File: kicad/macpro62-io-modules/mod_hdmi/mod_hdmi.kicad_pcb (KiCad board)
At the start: 2 copper layers, 43.4 x 9.4 mm, 5 parts, among them J1 MOD-H - HOAUC HYC79-HDMIA19-1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, J2 DF40C-50DP-0.4V(51) C424645 -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, U1 24C02 WLCSP-4 ID EEPROM @0x50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

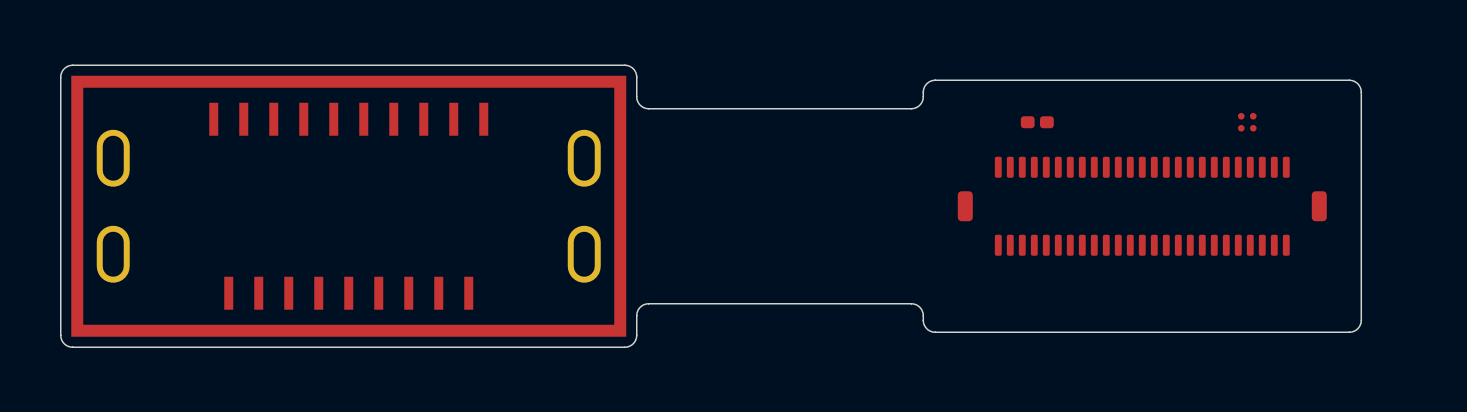
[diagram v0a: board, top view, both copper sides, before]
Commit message: I/O plate: centre + corner M1.6 frame screws, screwpt variant, plate fixes, module routing, ESD
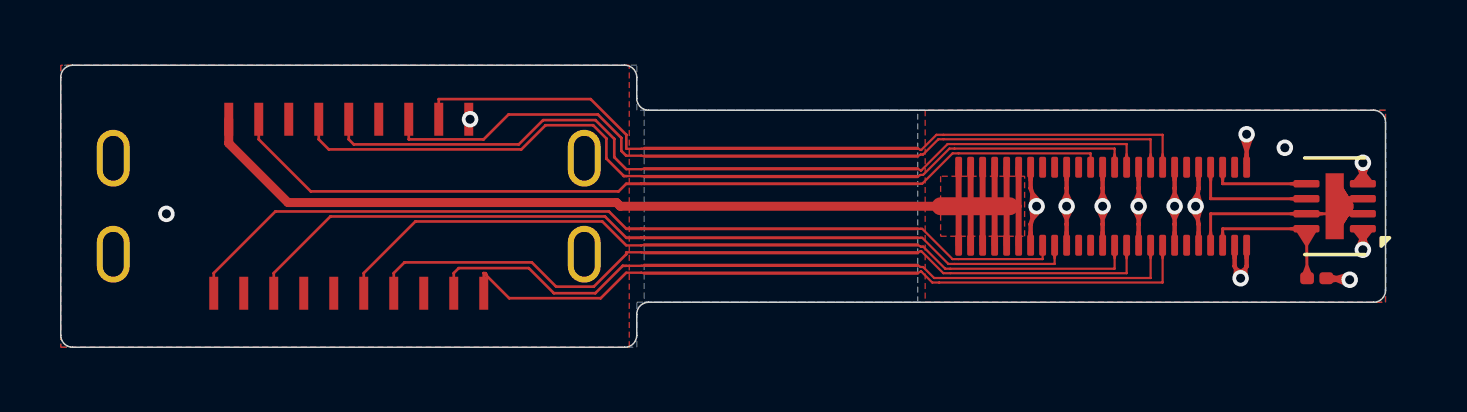
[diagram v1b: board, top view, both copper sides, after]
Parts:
- removed G1: sleeve GND ring (SUS304 0.2 sleeve, bonded to the shell), MP62_MOD:MP62_MOD_Sleeve_GND_Ring_HDMI
- C1: value 100nF 0201 (3V3_MOD) -> 100nF 0201 X5R 10V (3V3_MOD)
- J2: value DF40C-50DP-0.4V(51) C424645 -> main-board JMn DF40C-50DS (PMI-50 pinout) -> DF40C-50DP-0.4V(51) C424645 -> JMn DF40C-50DS (PMI-50 v2)
- U1: value 24C02 WLCSP-4 ID EEPROM @0x50 (MOD ID / type / rev / serial) -> BL24C02F-NTRC (C2828222) 24C02 ID EEPROM @0x50; footprint MP62_MOD:MP62_WLCSP-4_0.8x0.8_P0.4_EEPROM -> MP62_MOD:DFN-8-1EP_2x3mm_P0.5mm_EP0.61x2.2mm
- moved C1 10.7 mm to (132.3, 102.4)
- moved U1 4.04 mm to (132.9, 100.0), turned to 180 degrees
- moved J2 1.32 mm to (125.1, 100.0)
- turned J1 to 180 degrees
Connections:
- C1 pad 1: (no net) -> 3V3_MOD
- C1 pad 2: (no net) -> GND
- J1 pad 1: (no net) -> D2_P
- J1 pad 10: (no net) -> CK_P
- J1 pad 11: (no net) -> GND
- J1 pad 12: (no net) -> CK_N
- J1 pad 15: (no net) -> DDC_SCL
- J1 pad 16: (no net) -> DDC_SDA
- J1 pad 17: (no net) -> GND
- J1 pad 18: (no net) -> VBUS
- J1 pad 19: (no net) -> HPD
- J1 pad 2: (no net) -> GND
- J1 pad 3: (no net) -> D2_N
- J1 pad 4: (no net) -> D1_P
- J1 pad 5: (no net) -> GND
- J1 pad 6: (no net) -> D1_N
- J1 pad 7: (no net) -> D0_P
- J1 pad 8: (no net) -> GND
- J1 pad 9: (no net) -> D0_N
- J1 pad S: (no net) -> GND
- J2 pad 1: (no net) -> VBUS
- J2 pad 10: (no net) -> VBUS
- J2 pad 11: (no net) -> VBUS
- J2 pad 12: (no net) -> VBUS
- J2 pad 13: (no net) -> GND
- J2 pad 14: (no net) -> GND
- J2 pad 16: (no net) -> HPD
- J2 pad 18: (no net) -> DDC_SCL
- J2 pad 19: (no net) -> GND
- J2 pad 2: (no net) -> VBUS
- J2 pad 20: (no net) -> GND
- J2 pad 23: (no net) -> DDC_SDA
- J2 pad 25: (no net) -> GND
- J2 pad 26: (no net) -> GND
- J2 pad 27: (no net) -> CK_N
- J2 pad 28: (no net) -> D0_N
- J2 pad 29: (no net) -> CK_P
- J2 pad 3: (no net) -> VBUS
- J2 pad 30: (no net) -> D0_P
- J2 pad 31: (no net) -> GND
- J2 pad 32: (no net) -> GND
- J2 pad 33: (no net) -> D1_N
- J2 pad 34: (no net) -> D2_N
- J2 pad 35: (no net) -> D1_P
- J2 pad 36: (no net) -> D2_P
- J2 pad 37: (no net) -> GND
- J2 pad 38: (no net) -> GND
- J2 pad 4: (no net) -> VBUS
- J2 pad 41: (no net) -> GND
- J2 pad 42: (no net) -> GND
- J2 pad 43: (no net) -> ID_SCL
- J2 pad 44: (no net) -> GND
- J2 pad 45: (no net) -> ID_SDA
- J2 pad 46: (no net) -> 3V3_MOD
- J2 pad 48: (no net) -> GND
- J2 pad 49: (no net) -> GND
- J2 pad 5: (no net) -> VBUS
- J2 pad 50: (no net) -> GND
- J2 pad 6: (no net) -> VBUS
- J2 pad 7: (no net) -> VBUS
- J2 pad 8: (no net) -> VBUS
- J2 pad 9: (no net) -> VBUS
- U1 pad 1: (no net) -> GND
- U1 pad 2: (no net) -> GND
- U1 pad 3: (no net) -> GND
- U1 pad 4: (no net) -> GND
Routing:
- net VBUS: track 0.00 -> 43.6 mm
- net HPD: track 0.00 -> 30.3 mm
- net DDC_SDA: track 0.00 -> 30.1 mm
- net CK_N: track 0.00 -> 29.8 mm
- net CK_P: track 0.00 -> 29.2 mm
- net DDC_SCL: track 0.00 -> 28.8 mm
- net GND: track 0.00 -> 28.3 mm, vias 0 -> 14
- net D0_N: track 0.00 -> 27.8 mm
- net D1_N: track 0.00 -> 27.7 mm
- net D0_P: track 0.00 -> 27.3 mm
- net D1_P: track 0.00 -> 27.1 mm
- net D2_N: track 0.00 -> 26.0 mm
- net D2_P: track 0.00 -> 25.4 mm
- net 3V3_MOD: track 0.00 -> 5.00 mm
- net ID_SCL: track 0.00 -> 4.25 mm
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- added copper zone on B.Cu, net GND
- added copper zone on F.Cu, net GND
- added copper zone on F.Cu, net VBUS
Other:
- board size 43.4 x 9.4 mm -> 44.2 x 9.4 mm
- board text added: "C-fold 180 deg, R 2.74-2.74 = 14-14 x t (bend zone: no vias / parts, hatched L2)"
- board text added: "FR4 0.6 stiffener (B) under the header paddle"
- board text added: "FR4 1.0 stiffener (B, PSA) under the port"
- board text added: "cradle ledges (stiffener bottom bears here, 1.0 wide)"
- board text removed: "C-fold 180 deg, R 2.72 (bend zone: no vias, no parts, staggered traces)"
- board text removed: "FR4 1.0 stiffener (B) under the header paddle"
- board text removed: "FR4 1.0 stiffener (B, flush, PSA) under the port"
- board text removed: "Fits slots HDMI. Electrical length port pads -> header ~28 mm."
- board text removed: "MOD-H, unfolded. Port at (0,0); u -> outboard edge. Stiffener 19.2 x 9.4; tail 6.5 wide; flap 0.5; fold R 2.72; paddle 14.6 x 8.4."
- board text removed: "PMI-50 (J2 odd/even): 13/14 GND/GND; 15/16 GND/GND; 17/18 HS0_P/HS2_P; 19/20 HS0_N/HS2_N; 21/22 GND/GND; 23/24 HS1_P/HS3_P; 25/26 HS1_N/HS3_N; 27/28 GND/GND; 29/30 USB2_DP/SBU1; 31/32 USB2_DN/SBU2; 33/34 GND/GND; 35/36 CC1/HPD; 37/38 CC2/UTIL; 39/40 GND/GND; 41/42 ID_SCL/ID_SDA; 43/44 3V3_MOD/PRSNT#; 45/46 LED#/GND; 47/48 GND/GND; 49/50 GND/GND"
- board text removed: "Plug loads: push -> connector body -> FPC -> FR4 stiffener -> cradle ledges; pull/side -> bonded SUS sleeve -> collar -> clamp plate -> screws. Not through solder or flex."
- board text removed: "cradle ledges (stiffener bottom bears here; no parts / THT tips in the bands)"
- board text removed: "optional silver EMI film (F), >= 0.8 from stiffeners, GND openings D1.0 at both ends"

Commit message: USB-C flex module routed (HYCW417, 0 DRC, matched pairs), 3-mil min on flexes, two flex panels, CH334F + ASM1182e QFN-48 footprints
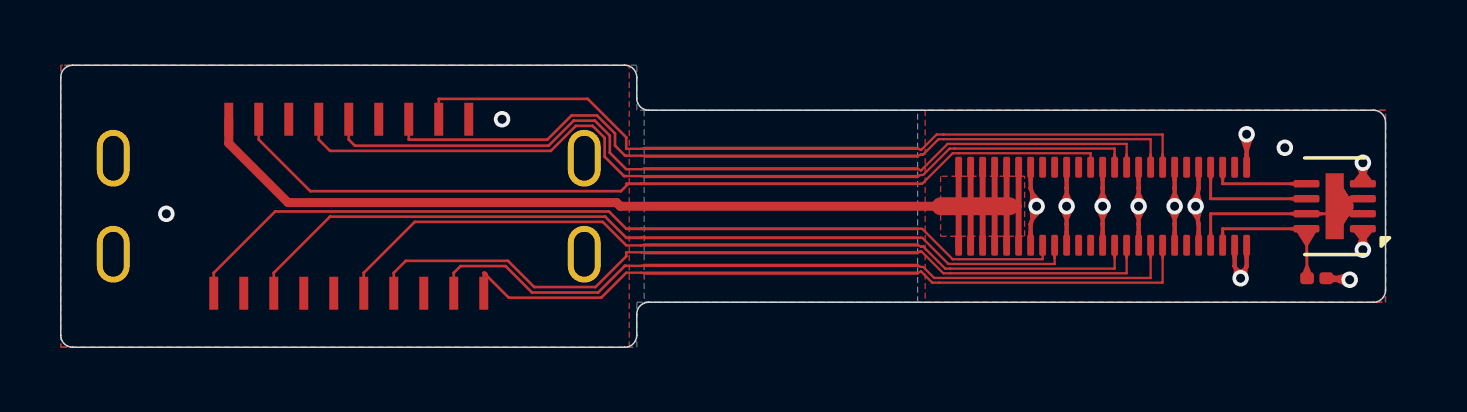
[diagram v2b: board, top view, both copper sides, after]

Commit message: Plate test-print fixes (corners +1mm Y, C2 post -1mm, C1 removed); USB-A/HDMI hand fan-out 0 skew; real DF40 + HDMI footprints
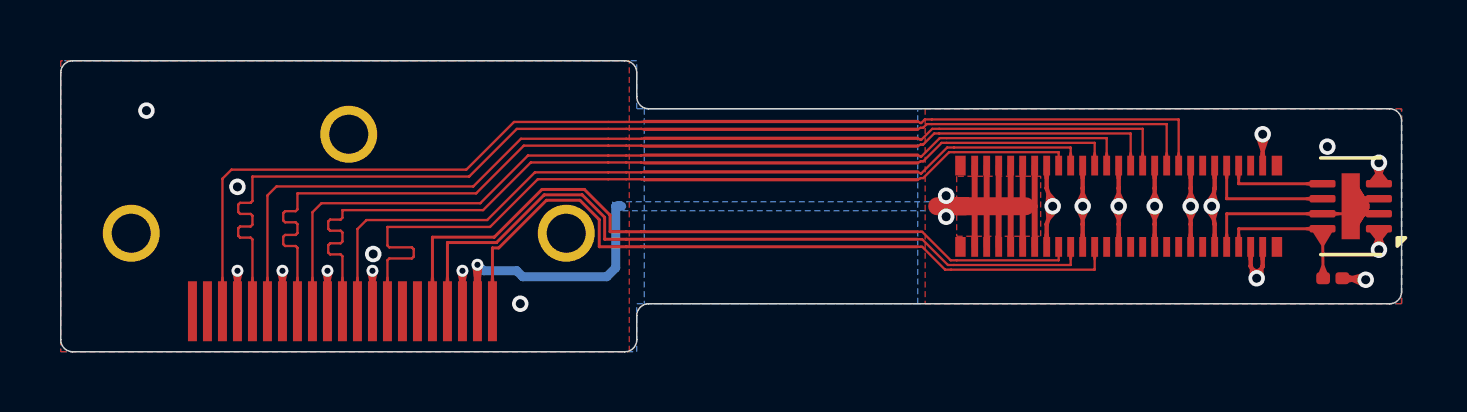
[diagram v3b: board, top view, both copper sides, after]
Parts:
- J1: value MOD-H - HOAUC HYC79-HDMIA19-105 (C711353) SMD + THT shell -> MOD-H - HOAUC HYC79-HDMIA19-105 (C711353) 19 SMD (1 row, 0.5) + 3 THT legs D1.3; footprint MP62_MOD:MP62_HDMI_A_Vertical_PLACEHOLDER -> MP62_MOD:HOAUC_HYC79-HDMIA19-105
- J2: footprint MP62_MOD:MP62_Hirose_DF40C-50DP-0.4V_PLACEHOLDER -> MP62_MOD:MP62_Hirose_DF40C-50DP-0.4V
- moved C1 0.53 mm to (132.8, 102.4)
- moved J2 0.53 mm to (125.7, 100.0)
- moved U1 0.53 mm to (133.4, 100.0)
- turned J1 to 0 degrees
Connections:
- J2 pad 15: (no net) -> CK_N
- J2 pad 16: HPD -> DDC_SCL
- J2 pad 17: (no net) -> CK_P
- J2 pad 18: DDC_SCL -> DDC_SDA
- J2 pad 21: (no net) -> D0_N
- J2 pad 22: (no net) -> HPD
- J2 pad 23: DDC_SDA -> D0_P
- J2 pad 27: CK_N -> D1_N
- J2 pad 28: D0_N -> (no net)
- J2 pad 29: CK_P -> D1_P
- J2 pad 30: D0_P -> (no net)
- J2 pad 33: D1_N -> D2_N
- J2 pad 34: D2_N -> (no net)
- J2 pad 35: D1_P -> D2_P
- J2 pad 36: D2_P -> (no net)
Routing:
- net VBUS: track 43.6 -> 28.2 mm, vias 0 -> 3
- net D2_P: track 25.4 -> 38.7 mm
- net D2_N: track 26.0 -> 38.7 mm
- net D1_P: track 27.0 -> 35.2 mm
- net D1_N: track 27.7 -> 35.2 mm
- net GND: track 28.3 -> 35.6 mm, vias 14 -> 21
- net HPD: track 30.3 -> 25.1 mm
- net DDC_SDA: track 30.2 -> 25.7 mm
- net D0_P: track 27.4 -> 31.7 mm
- net D0_N: track 27.8 -> 31.7 mm
- net DDC_SCL: track 28.8 -> 25.8 mm
- net CK_N: track 29.8 -> 28.3 mm
- net CK_P: track 29.2 -> 28.3 mm
- added copper zone on B.Cu, net VBUS
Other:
- board size 44.2 x 9.4 mm -> 44.7 x 9.7 mm
